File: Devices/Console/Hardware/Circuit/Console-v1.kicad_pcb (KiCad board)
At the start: 2 copper layers, 96.8 x 60 mm, 30 parts, among them J1 AVR-ISP-6, J2 TYPE-C-31-M-12, J3 Conn_01x13, J4 Conn_01x04, J5 Conn_01x04, SW1 PEC11R-4220F-S0012, SW2 PEC11R-4220F-S0012, SW3 PEC11R-4220F-S0012, SW4 PEC11R-4220F-S0012, SW5 SW_Push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

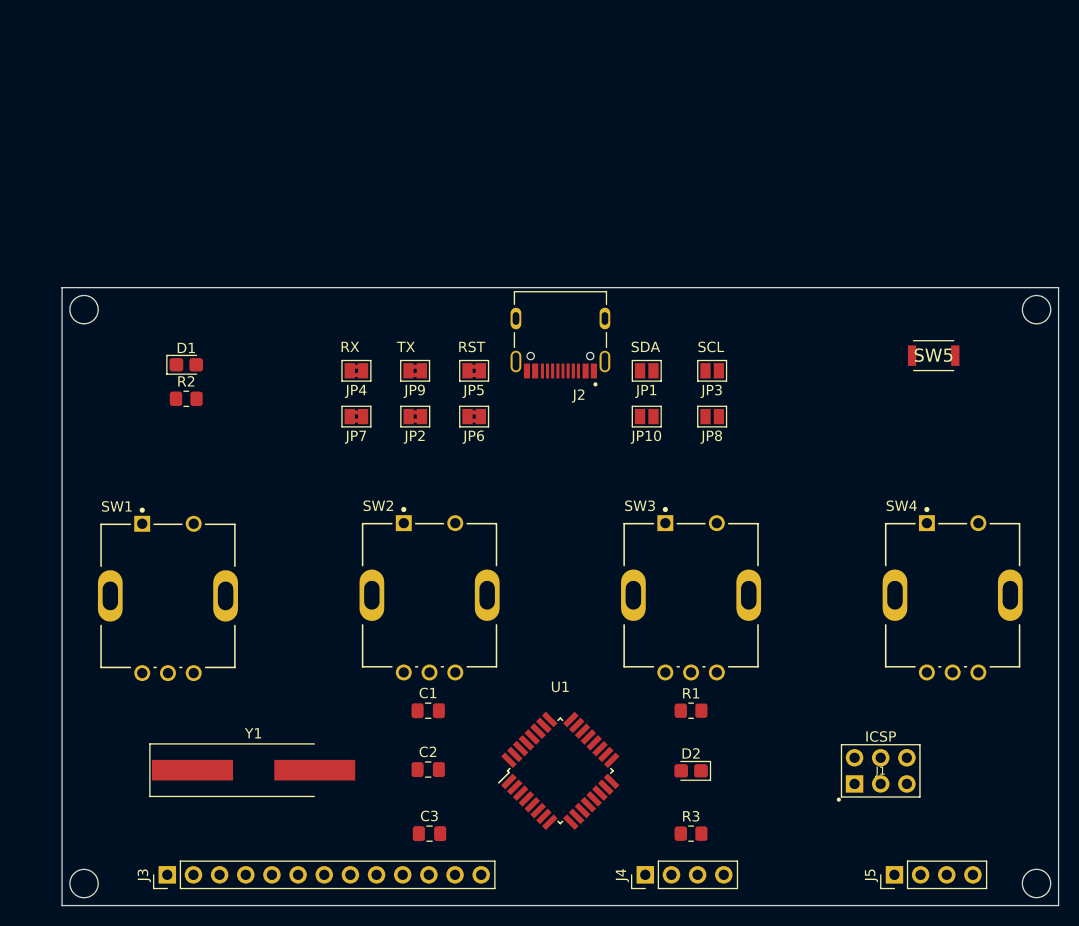
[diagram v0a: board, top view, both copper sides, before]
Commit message: Add second more centered pcb layout
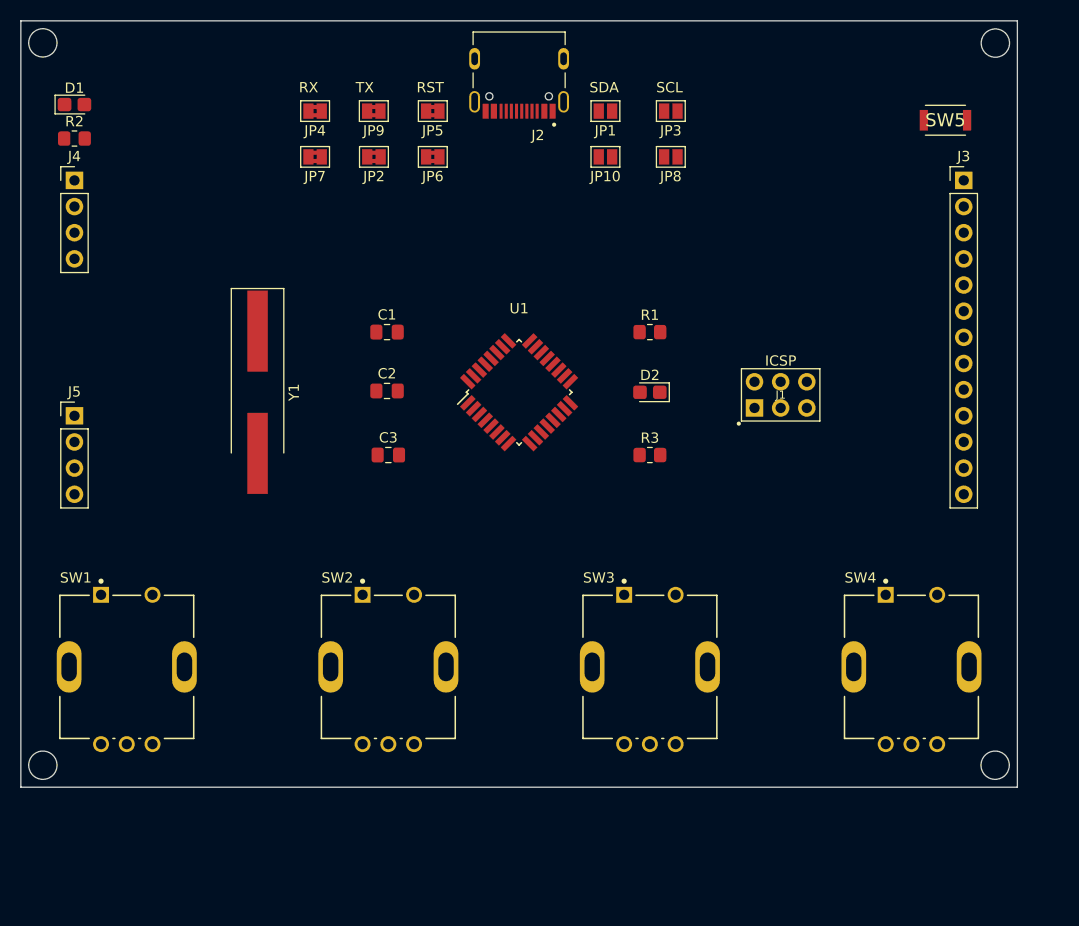
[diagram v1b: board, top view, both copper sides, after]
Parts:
- moved J3 102.6 mm to (185.4, 54.4), turned to 0 degrees
- moved J5 91.3 mm to (99.1, 77.2), turned to 0 degrees
- moved J4 87.3 mm to (99.1, 54.4), turned to 0 degrees
- moved J1 37.8 mm to (167.6, 75.2)
- moved C3 37.0 mm to (129.5, 81.0)
- moved C1 37.0 mm to (129.4, 69.1)
- moved C2 37.0 mm to (129.4, 74.8)
- moved R1 37.0 mm to (154.9, 69.1)
- moved R3 37.0 mm to (154.9, 81.0)
- moved D2 37.0 mm to (154.9, 74.9)
- moved U1 37.0 mm to (142.2, 74.9)
- moved Y1 36.7 mm to (116.8, 74.9), turned to 270 degrees
- moved D1 27.5 mm to (99.1, 47.0)
- moved R2 27.5 mm to (99.1, 50.3)
- moved J2 25.5 mm to (142.2, 42.5)
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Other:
- board size 96.8 x 60 mm -> 96.8 x 74.4 mm
